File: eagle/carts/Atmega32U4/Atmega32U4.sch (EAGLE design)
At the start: 30 parts, among them J6 USB4110-GF-A_REVB, U1 3.3V, U3 32U4, X3 16MHz

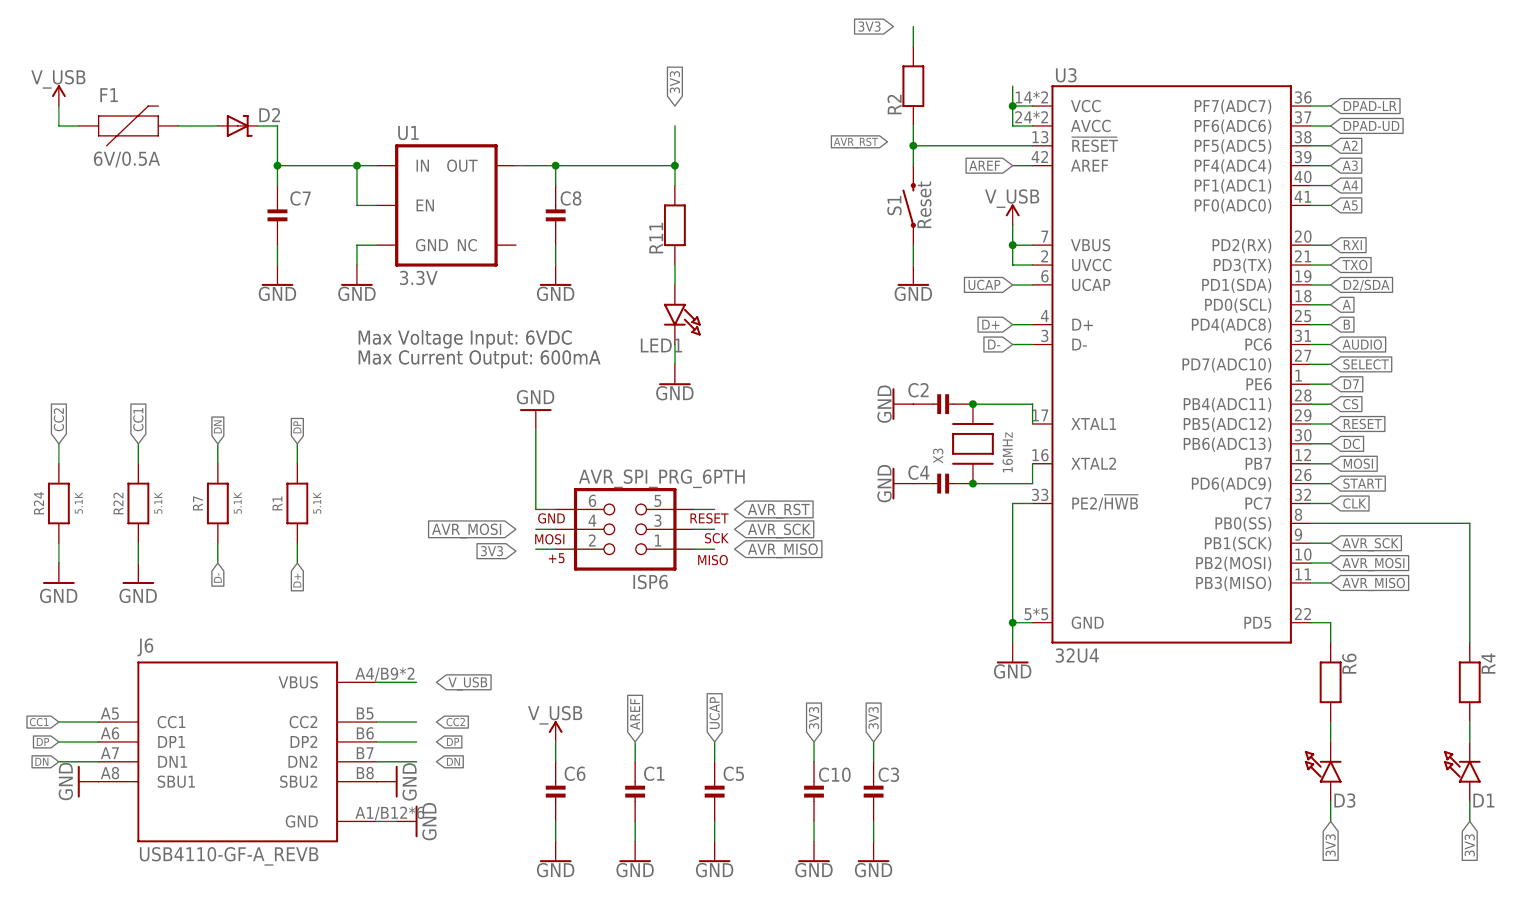
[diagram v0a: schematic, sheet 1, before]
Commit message: feat: update USB and VCC lines on ATMega
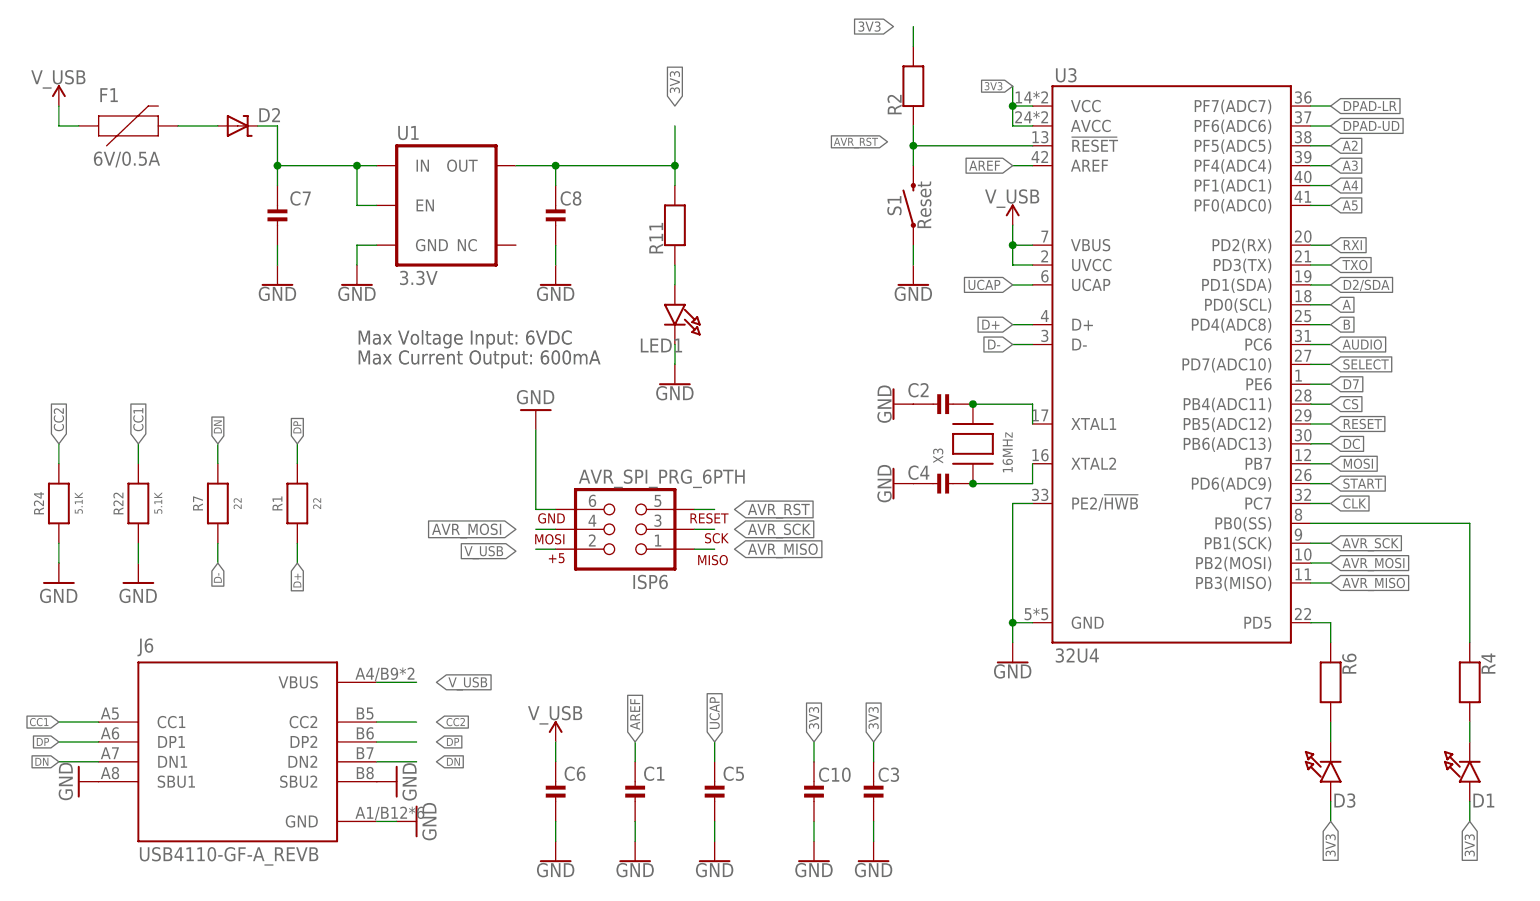
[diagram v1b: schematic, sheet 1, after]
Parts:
- R1, R7: value 5.1K -> 22; MPN ERJ-PA3F5101V -> ERJ-3EKF22R0V
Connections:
- net 3V3: no longer ISP6.2
- net V_USB: now also ISP6.2
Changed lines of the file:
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@@
 <attribute name="MPN" value="ERJ-PA3F5101V"/>
 </part>
-<part name="R1" library="RetroESP32" library_urn="urn:adsk.eagle:library:12566846" deviceset="RESISTOR" device="0603MINI" package3d_urn="urn:adsk.eagle:package:12566926/2" override_package3d_urn="urn:adsk.eagle:package:12547690/2" override_package_urn="urn:adsk.eagle:footprint:12547691/1" override_locally_modified="yes" value="5.1K">
-<attribute name="MPN" value="ERJ-PA3F5101V"/>
+<part name="R1" library="RetroESP32" library_urn="urn:adsk.eagle:library:12566846" deviceset="RESISTOR" device="0603MINI" package3d_urn="urn:adsk.eagle:package:12566926/2" override_package3d_urn="urn:adsk.eagle:package:12547690/2" override_package_urn="urn:adsk.eagle:footprint:12547691/1" override_locally_modified="yes" value="22">
+<attribute name="MPN" value="ERJ-3EKF22R0V"/>
 </part>
-<part name="R7" library="RetroESP32" library_urn="urn:adsk.eagle:library:12566846" deviceset="RESISTOR" device="0603MINI" package3d_urn="urn:adsk.eagle:package:12566926/2" override_package3d_urn="urn:adsk.eagle:package:12547690/2" override_package_urn="urn:adsk.eagle:footprint:12547691/1" override_locally_modified="yes" value="5.1K">
-<attribute name="MPN" value="ERJ-PA3F5101V"/>
+<part name="R7" library="RetroESP32" library_urn="urn:adsk.eagle:library:12566846" deviceset="RESISTOR" device="0603MINI" package3d_urn="urn:adsk.eagle:package:12566926/2" override_package3d_urn="urn:adsk.eagle:package:12547690/2" override_package_urn="urn:adsk.eagle:footprint:12547691/1" override_locally_modified="yes" value="22">
+<attribute name="MPN" value="ERJ-3EKF22R0V"/>
 </part>
 <part name="X3" library="adaprog" deviceset="XTAL" device="NX5032" value="16MHz"/>
@@
 <label x="60.96" y="33.02" size="1.27" layer="95" xref="yes"/>
 </segment>
+<segment>
+<wire x1="76.2" y1="50.038" x2="73.66" y2="50.038" width="0.1524" layer="91"/>
+<pinref part="ISP6" gate="G$1" pin="2"/>
+<label x="71.12" y="49.784" size="1.27" layer="95" rot="R180" xref="yes"/>
+</segment>
 </net>
 <net name="UCAP" class="0">
@@
 <wire x1="134.62" y1="104.14" x2="134.62" y2="106.68" width="0.1524" layer="91"/>
 <junction x="134.62" y="106.68"/>
+<label x="134.62" y="109.22" size="1.016" layer="95" rot="R180" xref="yes"/>
 </segment>
 <segment>
@@
 </segment>
 <segment>
-<wire x1="76.2" y1="50.038" x2="73.66" y2="50.038" width="0.1524" layer="91"/>
-<pinref part="ISP6" gate="G$1" pin="2"/>
-<label x="71.12" y="49.784" size="1.27" layer="95" rot="R180" xref="yes"/>
-</segment>
-<segment>

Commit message: feat: redesign ATmega cartridge
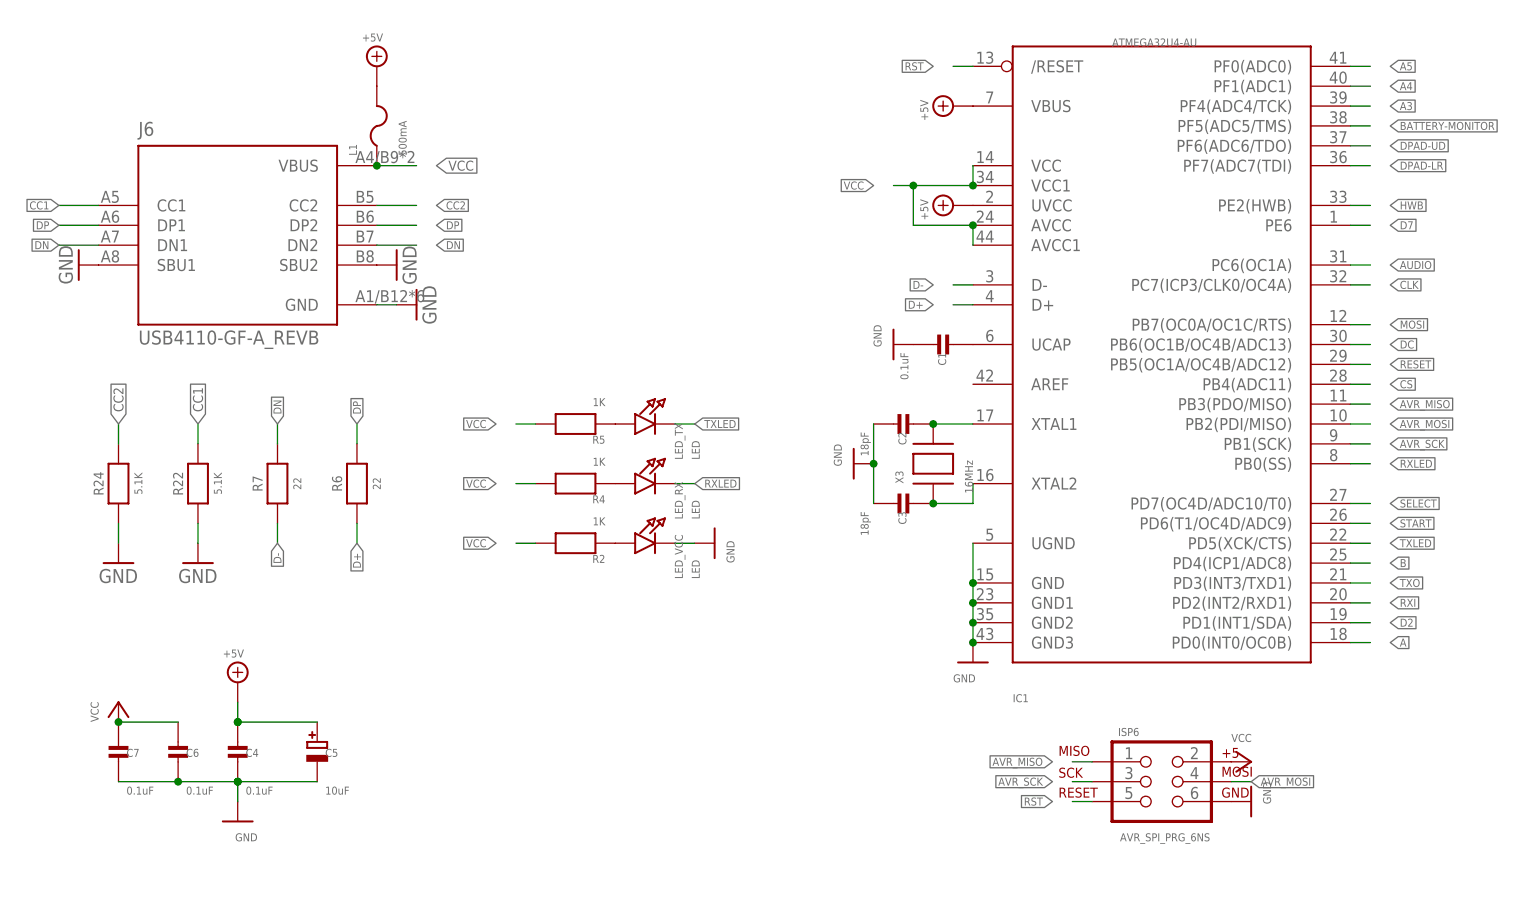
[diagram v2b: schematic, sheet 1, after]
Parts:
- removed C10: 1.0uF, RetroESP32:CAP_CERAMIC
- removed C8: 10uF, RetroESP32:CAP_CERAMIC
- removed D1: Yellow, RetroESP32:LED0603
- removed D2: 3A/10V/280mV, RetroESP32:DIODE-SCHOTTKYSOD-123
- removed D3: GREEN, RetroESP32:LED0603
- removed F1: 6V/0.5A, SparkFun-Fuses:PPTC_6V500MA-2
- removed LED1: RED, RetroESP32:LED0603
- removed R1: 22, RetroESP32:RESISTOR0603MINI
- removed R11: 1k, RetroESP32:RESISTOR0603MINI
- removed S1: Reset, SparkFun-Switches:MOMENTARY-SWITCH-SPST-SMD-4.6X2.8MM
- removed U1: 3.3V, SparkFun-IC-Power:V_REG_AP2112K-3.3V
- removed U3: 32U4, SparkFun-IC-Microcontroller:ATMEGA32U4TQFP-44
- added IC1: ATMEGA32U4-AU, adaprog:ATMEGA32U4-AU
- added L1: 500mA, adafruit:PTCFUSE-1206
- added LED_RX, LED_TX, LED_VCC: LED, RetroESP32:LED0603
- added R5: 1K, RetroESP32:RESISTOR0603MINI
- C2: value 22pF -> 18pF
- C3: value 0.1uF -> 18pF
- C4: value 22pF -> 0.1uF
- C5: value 1.0uF -> 10uF; device RetroESP32:CAP_CERAMIC -> RetroESP32:CAP_TANTALUMA/3216_WAVE
- C6: value 1.0uF -> 0.1uF
- C7: value 10uF -> 0.1uF
- ISP6: value AVR_SPI_PRG_6PTH -> AVR_SPI_PRG_6NS; device SparkFun-Connectors:AVR_SPI_PRG_6PTH -> SparkFun:AVR_SPI_PRG_6NS
- R2: value 10k -> 1K
- R4: value 1k -> 1K
- R6: value 1k -> 22; MPN (none) -> ERJ-3EKF22R0V
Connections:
- removed net 3V3: C10.2, C3.2, C8.2, D1.A, D3.A, R11.2, R2.2, U$2.3V3, U1.OUT, U3.AVCC@24, U3.VCC@14
- removed net A2: U3.PF5(ADC5)
- removed net AREF: C1.2, U3.AREF
- removed net AVR_RST: ISP6.5, R2.1, S1.2, U3.!RESET
- removed net D2/SDA: U3.PD1(SDA)
- removed net N$1: C2.1, U3.XTAL1, X3.P$2
- removed net N$38: LED1.A, R11.1
- removed net N$5: D1.C, R4.2
- removed net RAW: C7.2, D2.C, U1.EN, U1.IN
- removed net UCAP: C5.2, U3.UCAP
- removed net USB_RAW: D2.A, F1.2
- removed net V_USB: C6.2, F1.1, ISP6.2, J6.VBUS, U3.UVCC, U3.VBUS
- new net +5V: C4.1, C5.+, IC1.UVCC, IC1.VBUS, L1.2
- new net BATTERY-MONITOR: IC1.PF5(ADC5/TMS), U$2.AD0
- new net D2: IC1.PD1(INT1/SDA)
- new net HWB: IC1.PE2(HWB)
- new net N$4: C1.1, IC1.UCAP
- new net N$6: LED_RX.A, R4.1
- new net N$8: C2.1, IC1.XTAL1, X3.P$2
- new net N$9: C3.1, IC1.XTAL2, X3.P$1
- new net RST: IC1./RESET, ISP6.5
- new net VCC: C6.1, C7.1, IC1.AVCC, IC1.AVCC1, IC1.VCC, IC1.VCC1, ISP6.2, J6.VBUS, L1.1, R2.2, R4.2, R5.2, U$2.3V3
- net A: now also IC1.PD0(INT0/OC0B); no longer U3.PD0(SCL)
- net A3: now also IC1.PF4(ADC4/TCK); no longer U3.PF4(ADC4)
- net A4: now also IC1.PF1(ADC1); no longer U3.PF1(ADC1)
- net A5: now also IC1.PF0(ADC0); no longer U3.PF0(ADC0)
- net AUDIO: now also IC1.PC6(OC1A); no longer U3.PC6
- net AVR_MISO: now also IC1.PB3(PDO/MISO); no longer U3.PB3(MISO)
- net AVR_MOSI: now also IC1.PB2(PDI/MISO); no longer U3.PB2(MOSI)
- net AVR_SCK: now also IC1.PB1(SCK); no longer U3.PB1(SCK)
- net B: now also IC1.PD4(ICP1/ADC8); no longer U3.PD4(ADC8)
- net CLK: now also IC1.PC7(ICP3/CLK0/OC4A); no longer U3.PC7
- net CS: now also IC1.PB4(ADC11); no longer U3.PB4(ADC11)
- net D+: now also IC1.D+, R6.1; no longer R1.1, U3.D+
- net D-: now also IC1.D-; no longer U3.D-
- net D7: now also IC1.PE6; no longer U3.PE6
- net DC: now also IC1.PB6(OC1B/OC4B/ADC13); no longer U3.PB6(ADC13)
- net DP: now also R6.2; no longer R1.2
- net DPAD-LR: now also IC1.PF7(ADC7(TDI); no longer U3.PF7(ADC7)
- net DPAD-UD: now also IC1.PF6(ADC6/TDO); no longer U3.PF6(ADC6)
- net GND: now also C1.2, C3.2, C5.-, C6.2, C7.2, IC1.GND, IC1.GND1, IC1.GND2, IC1.GND3, IC1.UGND, LED_VCC.C; no longer C1.1, C10.1, C3.1, C5.1, C6.1, C7.1, C8.1, LED1.C, S1.1, U1.GND, U3.GND, U3.PE2/!HWB
- net MOSI: now also IC1.PB7(OC0A/OC1C/RTS); no longer U3.PB7
- net N$2: now also LED_VCC.A, R2.1; no longer C4.1, U3.XTAL2, X3.P$1
- net N$7: now also LED_TX.A, R5.1; no longer D3.C, R6.2
- net RESET: now also IC1.PB5(OC1A/OC4B/ADC12); no longer U3.PB5(ADC12)
- net RXI: now also IC1.PD2(INT2/RXD1); no longer U3.PD2(RX)
- net RXLED: now also IC1.PB0(SS), LED_RX.C; no longer R4.1, U3.PB0(SS)
- net SELECT: now also IC1.PD7(OC4D/ADC10/T0); no longer U3.PD7(ADC10)
- net START: now also IC1.PD6(T1/OC4D/ADC9); no longer U3.PD6(ADC9)
- net TXLED: now also IC1.PD5(XCK/CTS), LED_TX.C; no longer R6.1, U3.PD5
- net TXO: now also IC1.PD3(INT3/TXD1); no longer U3.PD3(TX)
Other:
- note removed: "Max Current Output: 600mA"
- note removed: "Max Voltage Input: 6VDC"
- moved on the sheet: C1, C2, C3, C4, C6, C7, ISP6, J6, R2, R22, R24, R4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
